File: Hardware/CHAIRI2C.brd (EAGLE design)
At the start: 32 x 32 mm, 23 parts, among them IC1 DS3502, IC2 DS3502, J2 OUTPUT, J4 M06-PLAIN

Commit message: Changed I2C pullups from 10K to 4K7. Moved designators to improve readability.
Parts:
- R10, R9: value 22K -> 4K7
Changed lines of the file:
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@@
 <element name="J2" library="SuperHouse-Connectors" library_urn="urn:adsk.eagle:library:11765989" package="DB9-PCB-SOCKET" package3d_urn="urn:adsk.eagle:package:17411309/2" value="OUTPUT" x="16" y="25" smashed="yes">
 <attribute name="NAME" x="15.205" y="27.62" size="0.4064" layer="25" ratio="10"/>
-<attribute name="VALUE" x="15.31" y="28.415" size="0.4064" layer="27" ratio="10"/>
+<attribute name="VALUE" x="15.31" y="28.415" size="0.8128" layer="27" ratio="10"/>
 </element>
 <element name="C2" library="SuperHouse-DiscreteSemi" library_urn="urn:adsk.eagle:library:11768461" package="C0603" package3d_urn="urn:adsk.eagle:package:7066315/6" value="100nF" x="4" y="15" smashed="yes" rot="R180">
 <attribute name="NAME" x="4.889" y="14.492" size="0.4064" layer="25" font="vector" rot="R180"/>
-<attribute name="VALUE" x="2.484" y="15.5348" size="1.016" layer="27" font="vector"/>
+<attribute name="VALUE" x="2.184" y="15.5348" size="0.8128" layer="27" font="vector"/>
 </element>
 <element name="C1" library="SuperHouse-DiscreteSemi" library_urn="urn:adsk.eagle:library:11768461" package="C0603" package3d_urn="urn:adsk.eagle:package:7066315/6" value="100nF" x="28" y="15" smashed="yes" rot="R180">
 <attribute name="NAME" x="28.889" y="14.492" size="0.4064" layer="25" font="vector" rot="R180"/>
-<attribute name="VALUE" x="26.484" y="15.5348" size="1.016" layer="27" font="vector"/>
+<attribute name="VALUE" x="26.484" y="15.5348" size="0.8128" layer="27" font="vector"/>
 </element>
 <element name="R8" library="SuperHouse-DiscreteSemi" library_urn="urn:adsk.eagle:library:11768461" package="R0603" package3d_urn="urn:adsk.eagle:package:11768543/2" value="4K7" x="4" y="17" smashed="yes">
 <attribute name="NAME" x="3.111" y="17.508" size="0.4064" layer="25" font="vector"/>
-<attribute name="VALUE" x="5.516" y="16.4652" size="1.016" layer="27" font="vector" rot="R180"/>
+<attribute name="VALUE" x="2.684" y="17.5348" size="0.8128" layer="27" font="vector"/>
 </element>
 <element name="LED1" library="SuperHouse-LEDs" library_urn="urn:adsk.eagle:library:11790571" package="LED-0603" package3d_urn="urn:adsk.eagle:package:7066240/3" value="BLUE" x="4" y="19" smashed="yes">
 <attribute name="NAME" x="3.111" y="19.5588" size="0.4064" layer="25"/>
-<attribute name="VALUE" x="5.516" y="18.4652" size="1.016" layer="27" rot="R180"/>
+<attribute name="VALUE" x="2.484" y="19.5348" size="0.8128" layer="27"/>
 </element>
 <element name="IC1" library="SuperHouse-ICs" library_urn="urn:adsk.eagle:library:11768868" package="MSOP10" package3d_urn="urn:adsk.eagle:package:20803613/2" value="DS3502" x="11" y="13" smashed="yes" rot="R180">
 <attribute name="NAME" x="11" y="11.4" size="0.6096" layer="25" ratio="18" rot="R180" align="bottom-center"/>
-<attribute name="VALUE" x="11" y="15" size="0.4064" layer="27" ratio="10" rot="R180" align="bottom-center"/>
+<attribute name="VALUE" x="11" y="15.4" size="0.8128" layer="27" ratio="10" rot="R180" align="bottom-center"/>
 </element>
 <element name="IC2" library="SuperHouse-ICs" library_urn="urn:adsk.eagle:library:11768868" package="MSOP10" package3d_urn="urn:adsk.eagle:package:20803613/2" value="DS3502" x="21" y="13" smashed="yes" rot="R180">
 <attribute name="NAME" x="21" y="11.4" size="0.6096" layer="25" ratio="18" rot="R180" align="bottom-center"/>
-<attribute name="VALUE" x="21" y="15" size="0.4064" layer="27" ratio="10" rot="R180" align="bottom-center"/>
+<attribute name="VALUE" x="21" y="15.4" size="0.8128" layer="27" ratio="10" rot="R180" align="bottom-center"/>
 </element>
 <element name="R1" library="SuperHouse-DiscreteSemi" library_urn="urn:adsk.eagle:library:11768461" package="R0603" package3d_urn="urn:adsk.eagle:package:11768543/2" value="22K" x="11" y="18" smashed="yes" rot="R270">
 <attribute name="NAME" x="11.508" y="18.889" size="0.4064" layer="25" font="vector" rot="R270"/>
-<attribute name="VALUE" x="10.0348" y="19.016" size="0.4064" layer="27" font="vector" rot="R270"/>
+<attribute name="VALUE" x="10.184" y="15.8348" size="0.8128" layer="27" font="vector"/>
 </element>
 <element name="R2" library="SuperHouse-DiscreteSemi" library_urn="urn:adsk.eagle:library:11768461" package="R0603" package3d_urn="urn:adsk.eagle:package:11768543/2" value="22K" x="9" y="18" smashed="yes" rot="R90">
 <attribute name="NAME" x="8.492" y="17.111" size="0.4064" layer="25" font="vector" rot="R90"/>
-<attribute name="VALUE" x="9.9652" y="16.984" size="0.4064" layer="27" font="vector" rot="R90"/>
+<attribute name="VALUE" x="8.084" y="19.4348" size="0.8128" layer="27" font="vector"/>
 </element>
 <element name="R3" library="SuperHouse-DiscreteSemi" library_urn="urn:adsk.eagle:library:11768461" package="R0603" package3d_urn="urn:adsk.eagle:package:11768543/2" value="22K" x="19" y="18" smashed="yes" rot="R90">
 <attribute name="NAME" x="18.492" y="17.111" size="0.4064" layer="25" font="vector" rot="R90"/>
-<attribute name="VALUE" x="19.9652" y="16.984" size="0.4064" layer="27" font="vector" rot="R90"/>
+<attribute name="VALUE" x="17.884" y="19.4348" size="0.8128" layer="27" font="vector"/>
 </element>
 <element name="R4" library="SuperHouse-DiscreteSemi" library_urn="urn:adsk.eagle:library:11768461" package="R0603" package3d_urn="urn:adsk.eagle:package:11768543/2" value="22K" x="13" y="18" smashed="yes" rot="R270">
 <attribute name="NAME" x="13.508" y="18.889" size="0.4064" layer="25" font="vector" rot="R270"/>
-<attribute name="VALUE" x="12.0348" y="19.016" size="0.4064" layer="27" font="vector" rot="R270"/>
+<attribute name="VALUE" x="12.284" y="19.4348" size="0.8128" layer="27" font="vector"/>
 </element>
 <element name="R5" library="SuperHouse-DiscreteSemi" library_urn="urn:adsk.eagle:library:11768461" package="R0603" package3d_urn="urn:adsk.eagle:package:11768543/2" value="1K" x="23" y="18" smashed="yes" rot="R270">
 <attribute name="NAME" x="23.508" y="18.889" size="0.4064" layer="25" font="vector" rot="R270"/>
-<attribute name="VALUE" x="22.0348" y="19.016" size="0.4064" layer="27" font="vector" rot="R270"/>
+<attribute name="VALUE" x="22.184" y="19.4348" size="0.8128" layer="27" font="vector"/>
 </element>
 <element name="R6" library="SuperHouse-DiscreteSemi" library_urn="urn:adsk.eagle:library:11768461" package="R0603" package3d_urn="urn:adsk.eagle:package:11768543/2" value="1K" x="21" y="18" smashed="yes" rot="R90">
 <attribute name="NAME" x="20.492" y="17.111" size="0.4064" layer="25" font="vector" rot="R90"/>
-<attribute name="VALUE" x="21.9652" y="16.984" size="0.4064" layer="27" font="vector" rot="R90"/>
+<attribute name="VALUE" x="20.284" y="19.4348" size="0.8128" layer="27" font="vector"/>
 </element>
 <element name="R7" library="SuperHouse-DiscreteSemi" library_urn="urn:adsk.eagle:library:11768461" package="R0603" package3d_urn="urn:adsk.eagle:package:11768543/2" value="4K7" x="28" y="17" smashed="yes">
 <attribute name="NAME" x="27.111" y="17.508" size="0.4064" layer="25" font="vector"/>
-<attribute name="VALUE" x="26.984" y="16.0348" size="0.4064" layer="27" font="vector"/>
+<attribute name="VALUE" x="27.484" y="17.6348" size="0.8128" layer="27" font="vector"/>
 </element>
 <element name="LED2" library="SuperHouse-LEDs" library_urn="urn:adsk.eagle:library:11790571" package="LED-0603" package3d_urn="urn:adsk.eagle:package:7066240/3" value="GREEN" x="28" y="19" smashed="yes">
 <attribute name="NAME" x="27.111" y="19.5588" size="0.4064" layer="25"/>
-<attribute name="VALUE" x="26.984" y="18.0348" size="0.4064" layer="27"/>
+<attribute name="VALUE" x="26.484" y="19.5348" size="0.8128" layer="27"/>
 </element>
-<element name="R9" library="SuperHouse-DiscreteSemi" library_urn="urn:adsk.eagle:library:11768461" package="R0603" package3d_urn="urn:adsk.eagle:package:11768543/2" value="22K" x="8" y="7" smashed="yes" rot="R180">
+<element name="R9" library="SuperHouse-DiscreteSemi" library_urn="urn:adsk.eagle:library:11768461" package="R0603" package3d_urn="urn:adsk.eagle:package:11768543/2" value="4K7" x="8" y="7" smashed="yes" rot="R180">
 <attribute name="NAME" x="8.889" y="6.492" size="0.4064" layer="25" font="vector" rot="R180"/>
-<attribute name="VALUE" x="9.016" y="7.9652" size="0.4064" layer="27" font="vector" rot="R180"/>
+<attribute name="VALUE" x="7.084" y="7.5348" size="0.8128" layer="27" font="vector"/>
 </element>
-<element name="R10" library="SuperHouse-DiscreteSemi" library_urn="urn:adsk.eagle:library:11768461" package="R0603" package3d_urn="urn:adsk.eagle:package:11768543/2" value="22K" x="8" y="9" smashed="yes" rot="R180">
+<element name="R10" library="SuperHouse-DiscreteSemi" library_urn="urn:adsk.eagle:library:11768461" package="R0603" package3d_urn="urn:adsk.eagle:package:11768543/2" value="4K7" x="8" y="9" smashed="yes" rot="R180">
 <attribute name="NAME" x="8.889" y="8.492" size="0.4064" layer="25" font="vector" rot="R180"/>
-<attribute name="VALUE" x="9.016" y="9.9652" size="0.4064" layer="27" font="vector" rot="R180"/>
+<attribute name="VALUE" x="7.084" y="9.5348" size="0.8128" layer="27" font="vector"/>
 </element>
 <element name="U$2" library="SuperHouse-Jumpers" library_urn="urn:adsk.eagle:library:12190622" package="SJC" package3d_urn="urn:adsk.eagle:package:7066342/1" value="PU" x="4" y="5" smashed="yes" rot="R180">
@@
 <element name="R11" library="SuperHouse-DiscreteSemi" library_urn="urn:adsk.eagle:library:11768461" package="R0603" package3d_urn="urn:adsk.eagle:package:11768543/2" value="22K" x="25" y="18" smashed="yes" rot="R270">
 <attribute name="NAME" x="25.508" y="18.889" size="0.4064" layer="25" font="vector" rot="R270"/>
-<attribute name="VALUE" x="24.0348" y="19.016" size="0.4064" layer="27" font="vector" rot="R270"/>
+<attribute name="VALUE" x="24.084" y="19.4348" size="0.8128" layer="27" font="vector"/>
 </element>
 <element name="J4" library="SuperHouse-Connectors" library_urn="urn:adsk.eagle:library:11765989" package="1X06" package3d_urn="urn:adsk.eagle:package:11818425/2" value="M06-PLAIN" x="16" y="4" smashed="yes">

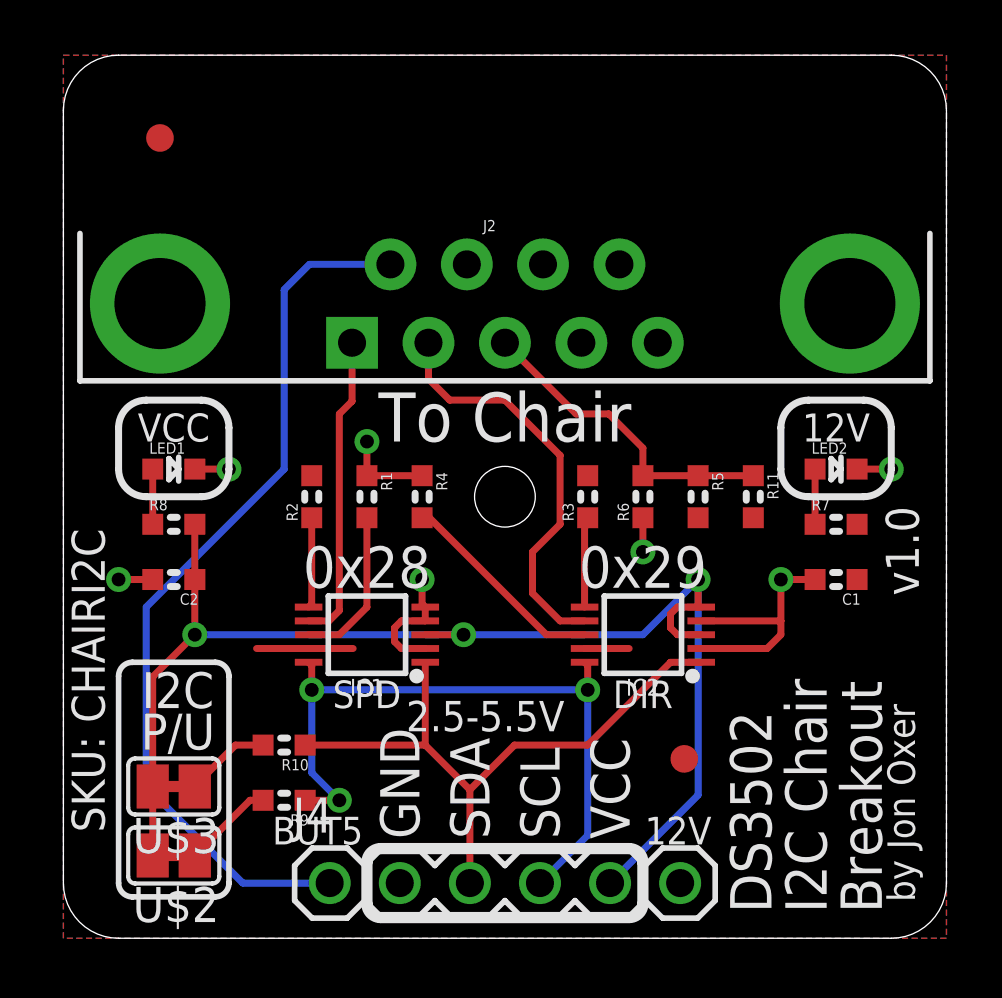
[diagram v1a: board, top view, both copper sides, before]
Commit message: Renumbered parts to simplify production setup.
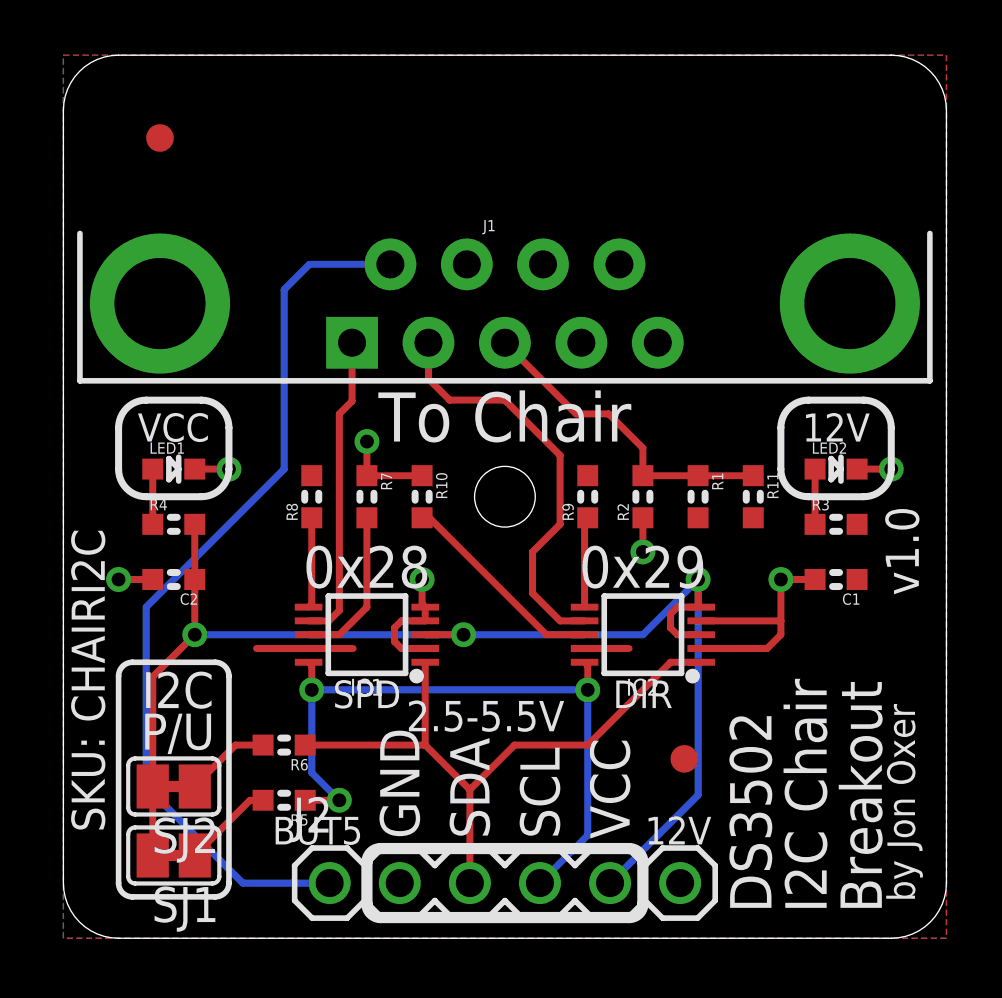
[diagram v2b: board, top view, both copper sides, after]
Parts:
- removed J4: M06-PLAIN, SuperHouse-Connectors:1X06
- added J1: OUTPUT, SuperHouse-Connectors:DB9-PCB-SOCKET
- J2: value OUTPUT -> M06-PLAIN; device SuperHouse-Connectors:DB9-PCB-SOCKET -> SuperHouse-Connectors:1X06
- R1, R2: value 22K -> 1K
- R10, R7, R8, R9: value 4K7 -> 22K
- R3, R4: value 22K -> 4K7
- R5, R6: value 1K -> 4K7
- moved J2 21.0 mm to (16.0, 4.00)
- moved R5 18.6 mm to (8.00, 7.00), turned to 180 degrees
- moved R7 17.0 mm to (11.0, 18.0), turned to 270 degrees
- moved R6 15.8 mm to (8.00, 9.00), turned to 180 degrees
- moved R9 15.6 mm to (19.0, 18.0), turned to 90 degrees
- moved R1 12.0 mm to (23.0, 18.0)
- moved R2 12.0 mm to (21.0, 18.0)
- moved R10 10.3 mm to (13.0, 18.0), turned to 270 degrees
- moved R3 9.06 mm to (28.0, 17.0), turned to 0 degrees
- moved R4 9.06 mm to (4.00, 17.0), turned to 0 degrees
- moved R8 5.10 mm to (9.00, 18.0), turned to 90 degrees
- renumbered U$2 to SJ1, U$3 to SJ2, U$8 to FID1, U$9 to FID2
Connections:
- net 12V: now also J1.7, J1.9, J2.6, R1.2, R8.2, R9.2; no longer J2.7, J2.9, J4.6, R2.2, R5.2, R7.2
- net BUT5: now also J1.6, J2.1; no longer J2.6, J4.1
- net DIRECTION_OUT: now also J1.2; no longer J2.2
- net GND: now also J1.5, J1.8, J2.2, R10.1, R2.1, R7.1; no longer J2.5, J2.8, J4.2, R1.1, R4.1, R6.1
- net N$1: now also R5.2; no longer R9.2
- net N$15: now also R10.2; no longer R4.2
- net N$2: now also R8.1; no longer R2.1
- net N$3: now also R9.1; no longer R3.1
- net N$4: now also R7.2; no longer R1.2
- net N$5: now also R4.1; no longer R8.1
- net N$6: now also R3.1; no longer R7.1
- net N$8: now also R6.2; no longer R10.2
- net SCL: now also J2.4, R5.1; no longer J4.4, R9.1
- net SDA: now also J2.3, R6.1; no longer J4.3, R10.1
- net SPEED_OUT: now also J1.1; no longer J2.1
- net VCC: now also J2.5, R4.2; no longer J4.5, R8.2
- net VREF: now also J1.3, R1.1, R2.2; no longer J2.3, R5.1, R6.2

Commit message: Changed output range resistors from 22K to 0R.
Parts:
- R10, R7, R8, R9: value 22K -> 0R
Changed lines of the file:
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@@
 <attribute name="VALUE" x="21" y="15.4" size="0.8128" layer="27" ratio="10" rot="R180" align="bottom-center"/>
 </element>
-<element name="R7" library="SuperHouse-DiscreteSemi" library_urn="urn:adsk.eagle:library:11768461" package="R0603" package3d_urn="urn:adsk.eagle:package:11768543/2" value="22K" x="11" y="18" smashed="yes" rot="R270">
+<element name="R7" library="SuperHouse-DiscreteSemi" library_urn="urn:adsk.eagle:library:11768461" package="R0603" package3d_urn="urn:adsk.eagle:package:11768543/2" value="0R" x="11" y="18" smashed="yes" rot="R270">
 <attribute name="NAME" x="11.508" y="18.889" size="0.4064" layer="25" font="vector" rot="R270"/>
 <attribute name="VALUE" x="10.184" y="15.8348" size="0.8128" layer="27" font="vector"/>
 </element>
-<element name="R8" library="SuperHouse-DiscreteSemi" library_urn="urn:adsk.eagle:library:11768461" package="R0603" package3d_urn="urn:adsk.eagle:package:11768543/2" value="22K" x="9" y="18" smashed="yes" rot="R90">
+<element name="R8" library="SuperHouse-DiscreteSemi" library_urn="urn:adsk.eagle:library:11768461" package="R0603" package3d_urn="urn:adsk.eagle:package:11768543/2" value="0R" x="9" y="18" smashed="yes" rot="R90">
 <attribute name="NAME" x="8.492" y="17.111" size="0.4064" layer="25" font="vector" rot="R90"/>
 <attribute name="VALUE" x="8.084" y="19.4348" size="0.8128" layer="27" font="vector"/>
 </element>
-<element name="R9" library="SuperHouse-DiscreteSemi" library_urn="urn:adsk.eagle:library:11768461" package="R0603" package3d_urn="urn:adsk.eagle:package:11768543/2" value="22K" x="19" y="18" smashed="yes" rot="R90">
+<element name="R9" library="SuperHouse-DiscreteSemi" library_urn="urn:adsk.eagle:library:11768461" package="R0603" package3d_urn="urn:adsk.eagle:package:11768543/2" value="0R" x="19" y="18" smashed="yes" rot="R90">
 <attribute name="NAME" x="18.492" y="17.111" size="0.4064" layer="25" font="vector" rot="R90"/>
 <attribute name="VALUE" x="17.884" y="19.4348" size="0.8128" layer="27" font="vector"/>
 </element>
-<element name="R10" library="SuperHouse-DiscreteSemi" library_urn="urn:adsk.eagle:library:11768461" package="R0603" package3d_urn="urn:adsk.eagle:package:11768543/2" value="22K" x="13" y="18" smashed="yes" rot="R270">
+<element name="R10" library="SuperHouse-DiscreteSemi" library_urn="urn:adsk.eagle:library:11768461" package="R0603" package3d_urn="urn:adsk.eagle:package:11768543/2" value="0R" x="13" y="18" smashed="yes" rot="R270">
 <attribute name="NAME" x="13.508" y="18.889" size="0.4064" layer="25" font="vector" rot="R270"/>
 <attribute name="VALUE" x="12.284" y="19.4348" size="0.8128" layer="27" font="vector"/>
